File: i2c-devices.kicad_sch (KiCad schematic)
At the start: 7 parts, among them IC17 AT24CS01-ST

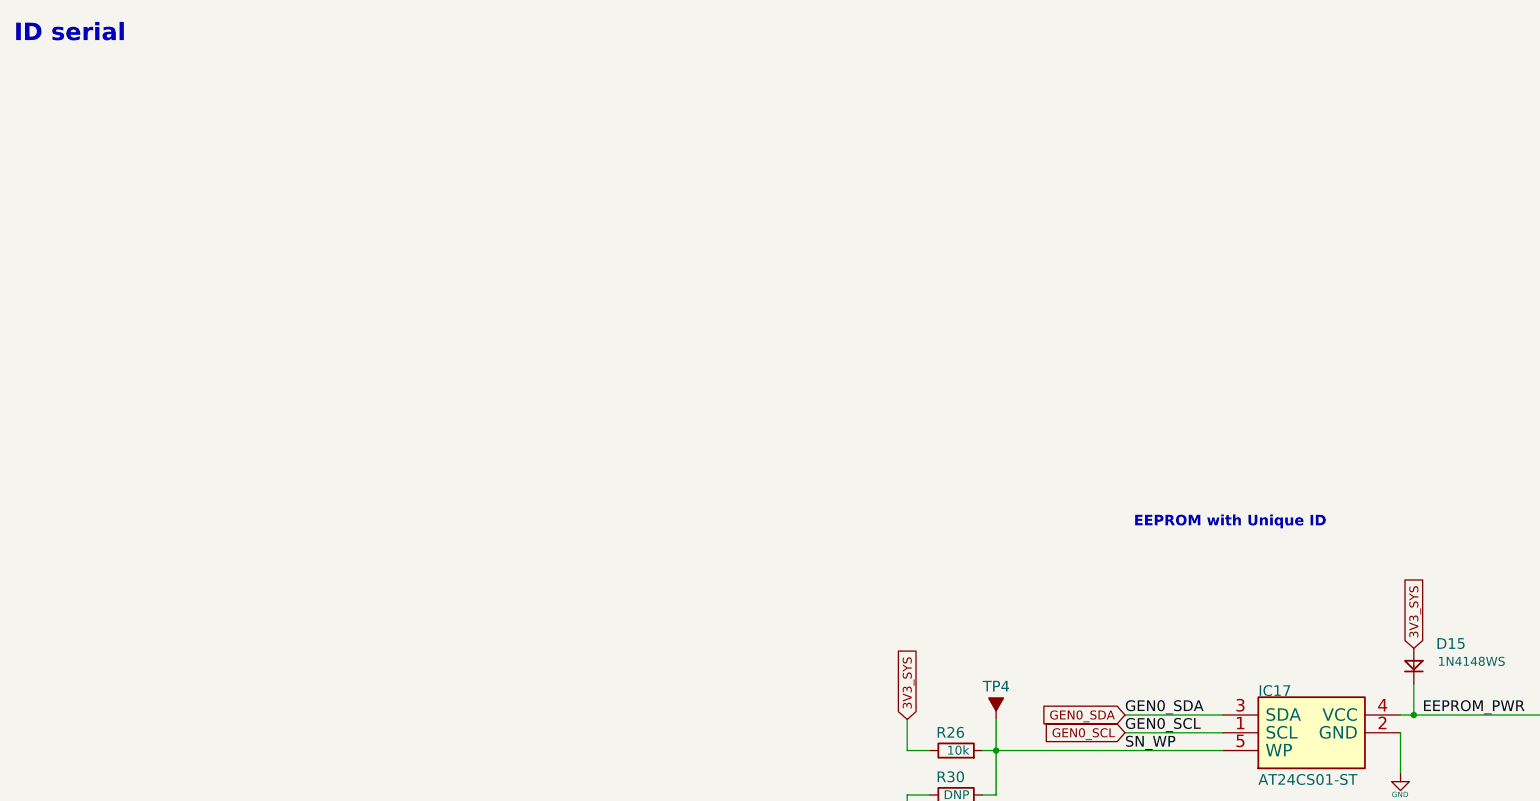
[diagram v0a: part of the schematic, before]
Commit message: Start of trigger FPGA.  Better layout
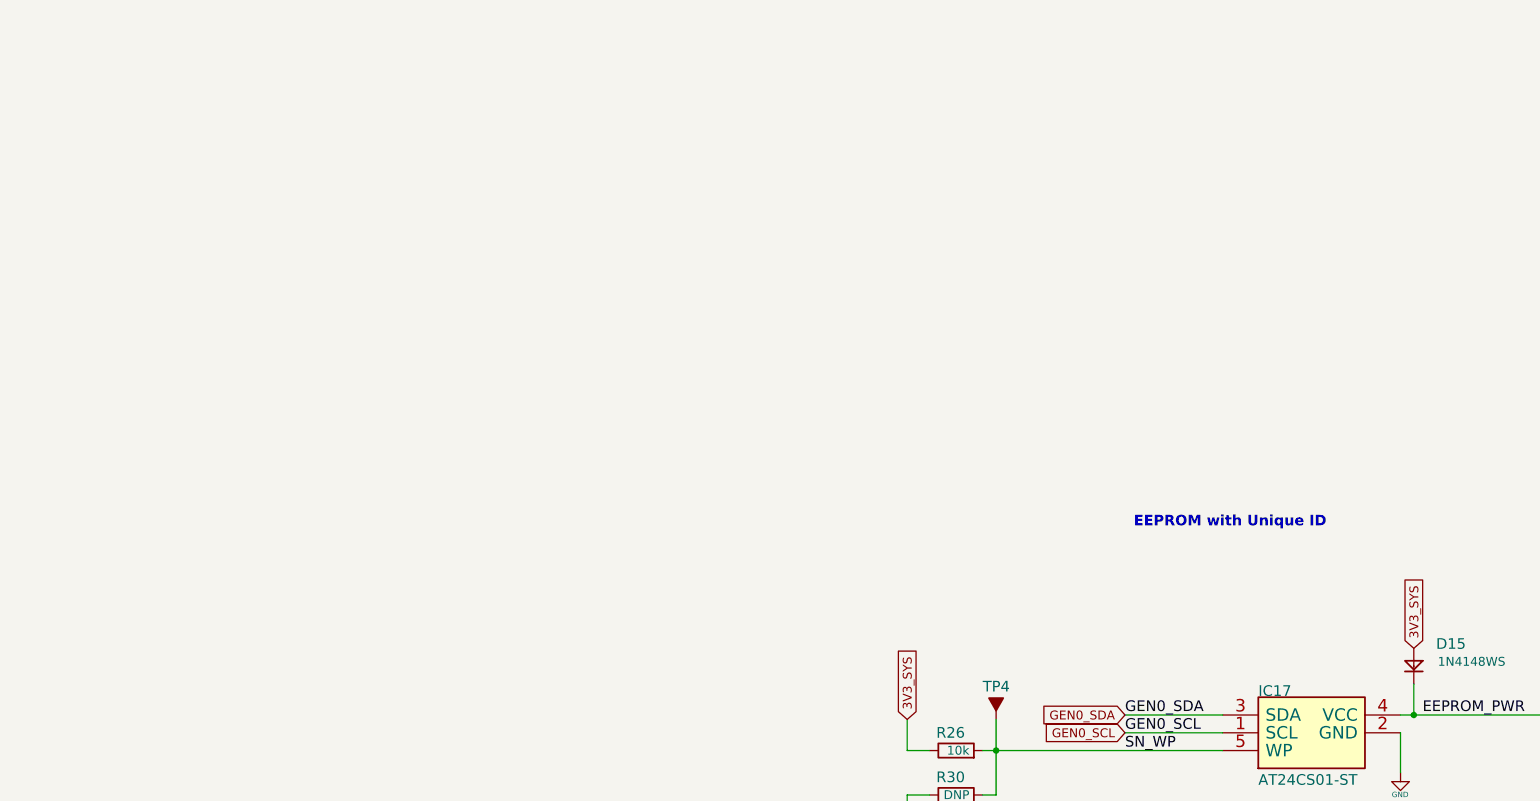
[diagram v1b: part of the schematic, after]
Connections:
- net EEPROM_PWR: now also D15.K; no longer D15.C
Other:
- note removed: "ID serial"
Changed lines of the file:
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@@
     (effects (font (size 1.4986 1.4986) (thickness 0.2997) bold) (justify left bottom))
-  )
-  (text "ID serial" (at 18.415 24.13 0)
-    (effects (font (size 2.4892 2.4892) (thickness 0.4978) bold) (justify left bottom))
   )
   (text "0x50h - memory" (at 197.5358 140.4366 0)
@@
   (symbol (lib_id "jetson-nano-baseboard:GND") (at 216.535 128.27 0) (unit 1)
     (in_bom yes) (on_board yes)
-    (property "Reference" "#GND_035" (id 0) (at 216.535 128.27 0)
+    (property "Reference" "#GND_028" (id 0) (at 216.535 128.27 0)
       (effects (font (size 0.508 0.508)) hide)
     )
@@
   (symbol (lib_id "jetson-nano-baseboard:GND") (at 247.65 143.51 0) (unit 1)
     (in_bom yes) (on_board yes)
-    (property "Reference" "#GND_0155" (id 0) (at 247.65 143.51 0)
+    (property "Reference" "#GND_029" (id 0) (at 247.65 143.51 0)
       (effects (font (size 0.508 0.508)) hide)
     )
@@
     (property "MPN" "1N4148WS" (id 5) (at 226.695 112.395 0))
     (pin "A")
-    (pin "C")
+    (pin "K")
   )
   (symbol (lib_id "jetson-nano-baseboard:C_100n_0402") (at 247.65 137.16 180) (unit 1)

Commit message: Checkpoint
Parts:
- removed D15: diode, jetson-nano-baseboard-footprints:SOD-323, symbol jetson-nano-baseboard:diode
- removed TP3: Testpad, jetson-nano-baseboard-footprints:TP-R-1.5, symbol jetson-nano-baseboard:Testpad
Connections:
- net EEPROM_PWR is gone; now on net 3V3_SYS: IC17.4 (VCC)
- net GEN0_SCL renamed I2C0_SCL
- net GEN0_SDA renamed I2C0_SDA
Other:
- moved on the sheet: C36

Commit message: Checkpoint
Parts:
- added R68, R69: DNP, jetson-nano-baseboard-footprints:0402-res, symbol jetson-nano-baseboard:R_2k_0402
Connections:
- net I2C0_SCL: now also R69.2
- net I2C0_SDA: now also R68.2
- new net EXTIO0: R68.1
- new net EXTIO1: R69.1
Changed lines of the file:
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@@
   (junction (at 218.44 115.824) (diameter 0) (color 0 0 0 0)
   )
+  (wire (pts (xy 175.895 156.21) (xy 177.8 156.21))
+    (stroke (width 0) (type default) (color 0 0 0 0))
+  )
   (wire (pts (xy 216.662 122.682) (xy 218.44 122.682))
     (stroke (width 0) (type default) (color 0 0 0 0))
@@
     (stroke (width 0) (type default) (color 0 0 0 0))
   )
+  (wire (pts (xy 175.895 159.385) (xy 177.8 159.385))
+    (stroke (width 0) (type default) (color 0 0 0 0))
+  )
   (polyline (pts (xy 807.5422 828.4972) (xy 810.4886 828.4972))
     (stroke (width 0) (type default) (color 0 0 0 0))
@@
     (stroke (width 0) (type default) (color 0 0 0 0))
   )
+  (wire (pts (xy 165.735 159.385) (xy 168.275 159.385))
+    (stroke (width 0) (type default) (color 0 0 0 0))
+  )
   (wire (pts (xy 218.44 115.824) (xy 218.44 120.142))
     (stroke (width 0) (type default) (color 0 0 0 0))
@@
   )
   (wire (pts (xy 223.266 115.824) (xy 218.44 115.824))
+    (stroke (width 0) (type default) (color 0 0 0 0))
+  )
+  (wire (pts (xy 165.735 156.21) (xy 168.275 156.21))
     (stroke (width 0) (type default) (color 0 0 0 0))
   )
@@
   (label "SN_WP" (at 177.292 125.222 0)
     (effects (font (size 1.524 1.524)) (justify left bottom))
+  )
+  (global_label "I2C0_SCL" (shape input) (at 177.8 159.385 0) (fields_autoplaced)
+    (effects (font (size 1.27 1.27)) (justify left))
+    (property "Intersheet References" "${INTERSHEET_REFS}" (id 0) (at 188.8932 159.4644 0)
+      (effects (font (size 1.27 1.27)) (justify left) hide)
+    )
   )
   (global_label "3V3_SYS" (shape input) (at 146.05 120.65 90) (fields_autoplaced)
@@
     (property "Intersheet References" "${INTERSHEET_REFS}" (id 0) (at -72.39 10.16 0)
       (effects (font (size 1.27 1.27)) hide)
+    )
+  )
+  (global_label "EXTIO0" (shape bidirectional) (at 165.735 156.21 180) (fields_autoplaced)
+    (effects (font (size 1.27 1.27)) (justify right))
+    (property "Intersheet References" "${INTERSHEET_REFS}" (id 0) (at 156.9398 156.2894 0)
+      (effects (font (size 1.27 1.27)) (justify right) hide)
+    )
+  )
+  (global_label "EXTIO1" (shape bidirectional) (at 165.735 159.385 180) (fields_autoplaced)
+    (effects (font (size 1.27 1.27)) (justify right))
+    (property "Intersheet References" "${INTERSHEET_REFS}" (id 0) (at 156.9398 159.4644 0)
+      (effects (font (size 1.27 1.27)) (justify right) hide)
+    )
+  )
+  (global_label "I2C0_SDA" (shape input) (at 177.8 156.21 0) (fields_autoplaced)
+    (effects (font (size 1.27 1.27)) (justify left))
+    (property "Intersheet References" "${INTERSHEET_REFS}" (id 0) (at 188.9537 156.2894 0)
+      (effects (font (size 1.27 1.27)) (justify left) hide)
     )
   )
@@
     (pin "1")
   )
+  (symbol (lib_id "jetson-nano-baseboard:R_2k_0402") (at 172.085 156.21 0) (unit 1)
+    (in_bom yes) (on_board yes)
+    (property "Reference" "R68" (id 0) (at 168.91 154.94 0)
+      (effects (font (size 1.524 1.524)) (justify right))
+    )
+    (property "Value" "DNP" (id 1) (at 172.085 160.02 0)
+      (effects (font (size 1.524 1.524)) hide)
+    )
+    (property "Footprint" "jetson-nano-baseboard-footprints:0402-res" (id 2) (at 177.165 151.13 0)
+      (effects (font (size 1.524 1.524)) (justify left) hide)
+    )
+    (property "Datasheet" "" (id 3) (at 172.085 156.21 0)
+      (effects (font (size 1.27 1.27)) hide)
+    )
+    (property "Manufacturer" "" (id 4) (at 177.165 146.05 0)
+      (effects (font (size 1.524 1.524)) (justify left) hide)
+    )
+    (property "MPN" "" (id 5) (at 177.165 148.59 0)
+      (effects (font (size 1.524 1.524)) (justify left) hide)
+    )
+    (property "Val" "DNP" (id 6) (at 173.99 156.21 0)
+      (effects (font (size 1.27 1.27)) (justify right))
+    )
+    (pin "1")
+    (pin "2")
+  )
   (symbol (lib_id "jetson-nano-baseboard:R_2k_0402") (at 153.162 125.222 0) (unit 1)
     (in_bom yes) (on_board yes)
@@
       (effects (font (size 1.27 1.27)) (justify right))
     )
+    (pin "1")
+    (pin "2")
+  )
+  (symbol (lib_id "jetson-nano-baseboard:R_2k_0402") (at 172.085 159.385 0) (unit 1)
+    (in_bom yes) (on_board yes)
+    (property "Reference" "R69" (id 0) (at 168.91 158.115 0)
+      (effects (font (size 1.524 1.524)) (justify right))
+    )
+    (property "Value" "DNP" (id 1) (at 172.085 163.195 0)
+      (effects (font (size 1.524 1.524)) hide)
+    )
+    (property "Footprint" "jetson-nano-baseboard-footprints:0402-res" (id 2) (at 177.165 154.305 0)
+      (effects (font (size 1.524 1.524)) (justify left) hide)
+    )
+    (property "Datasheet" "" (id 3) (at 172.085 159.385 0)
+      (effects (font (size 1.27 1.27)) hide)
+    )
+    (property "Manufacturer" "" (id 4) (at 177.165 149.225 0)
+      (effects (font (size 1.524 1.524)) (justify left) hide)
+    )
+    (property "MPN" "" (id 5) (at 177.165 151.765 0)
+      (effects (font (size 1.524 1.524)) (justify left) hide)
+    )
+    (property "Val" "DNP" (id 6) (at 173.99 159.385 0)
+      (effects (font (size 1.27 1.27)) (justify right))
+    )

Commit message: Checkpoint
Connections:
- net EXTIO0 renamed IO0/SDA
- net EXTIO1 renamed IO1/SCL
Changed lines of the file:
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@@
     (stroke (width 0) (type default) (color 0 0 0 0))
   )
-  (wire (pts (xy 165.735 159.385) (xy 168.275 159.385))
+  (wire (pts (xy 157.607 159.385) (xy 168.275 159.385))
     (stroke (width 0) (type default) (color 0 0 0 0))
   )
@@
     (stroke (width 0) (type default) (color 0 0 0 0))
   )
-  (wire (pts (xy 165.735 156.21) (xy 168.275 156.21))
+  (wire (pts (xy 157.607 156.21) (xy 168.275 156.21))
     (stroke (width 0) (type default) (color 0 0 0 0))
   )
@@
     )
   )
-  (global_label "EXTIO0" (shape bidirectional) (at 165.735 156.21 180) (fields_autoplaced)
+  (global_label "IO0{slash}SDA" (shape bidirectional) (at 157.607 156.21 180) (fields_autoplaced)
     (effects (font (size 1.27 1.27)) (justify right))
-    (property "Intersheet References" "${INTERSHEET_REFS}" (id 0) (at 156.9398 156.2894 0)
+    (property "Intersheet References" "${INTERSHEET_REFS}" (id 0) (at 147.2395 156.1306 0)
       (effects (font (size 1.27 1.27)) (justify right) hide)
     )
   )
-  (global_label "EXTIO1" (shape bidirectional) (at 165.735 159.385 180) (fields_autoplaced)
+  (global_label "IO1{slash}SCL" (shape bidirectional) (at 157.607 159.385 180) (fields_autoplaced)
     (effects (font (size 1.27 1.27)) (justify right))
-    (property "Intersheet References" "${INTERSHEET_REFS}" (id 0) (at 156.9398 159.4644 0)
+    (property "Intersheet References" "${INTERSHEET_REFS}" (id 0) (at 147.2999 159.3056 0)
       (effects (font (size 1.27 1.27)) (justify right) hide)
     )

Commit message: Checkpoint
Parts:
- R68: Val DNP -> 0
- R69: value DNP -> 0; Val DNP -> 0
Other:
- moved on the sheet: C36, IC17, R26, R30, R68, R69, TP4

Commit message: Checkpoint before v120 changes
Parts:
- R68: value DNP -> R_0R_0402; Val 0 -> 0R
- R69: value 0 -> R_0R_0402; Val 0 -> 0R
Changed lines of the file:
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@@
       (effects (font (size 1.524 1.524)) (justify right))
     )
-    (property "Value" "DNP" (id 1) (at 64.643 97.536 0)
+    (property "Value" "R_0R_0402" (id 1) (at 64.643 97.536 0)
       (effects (font (size 1.524 1.524)) hide)
     )
@@
       (effects (font (size 1.524 1.524)) (justify left) hide)
     )
-    (property "Val" "0" (id 6) (at 66.548 93.726 0)
+    (property "Val" "0R" (id 6) (at 66.548 93.726 0)
       (effects (font (size 1.27 1.27)) (justify right))
     )
@@
       (effects (font (size 1.524 1.524)) (justify right))
     )
-    (property "Value" "0" (id 1) (at 64.643 100.711 0)
+    (property "Value" "R_0R_0402" (id 1) (at 64.643 100.711 0)
       (effects (font (size 1.524 1.524)) hide)
     )
@@
       (effects (font (size 1.524 1.524)) (justify left) hide)
     )
-    (property "Val" "0" (id 6) (at 66.548 96.901 0)
+    (property "Val" "0R" (id 6) (at 66.548 96.901 0)
       (effects (font (size 1.27 1.27)) (justify right))
     )

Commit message: Resolve #14 by adding edge debug interface to MCU.  Change test pads and ESD parts.
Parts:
- TP4: footprint jetson-nano-baseboard-footprints:TP-R-1.5 -> TestPoint:TestPoint_Pad_D1.0mm
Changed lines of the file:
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@@
       (effects (font (size 1.524 1.524)) hide)
     )
-    (property "Footprint" "jetson-nano-baseboard-footprints:TP-R-1.5" (id 2) (at 52.578 59.182 0)
+    (property "Footprint" "TestPoint:TestPoint_Pad_D1.0mm" (id 2) (at 52.578 59.182 0)
       (effects (font (size 1.524 1.524)) hide)
     )
